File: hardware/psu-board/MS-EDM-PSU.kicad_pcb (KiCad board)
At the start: 4 copper layers, 150 x 95 mm, 42 parts, among them J1 HV_DC_IN__60-120V, J2 GAP_OUT__wire_work, J3 CAN, J4 LOGIC_5V_IN, J5 SWD, J6 NTC_TEMP, Q1 SiC_MOSFET, U1 STM32G474, U10 ISO_GATE_DRIVER, U11 ISO_CURRENT_AMP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

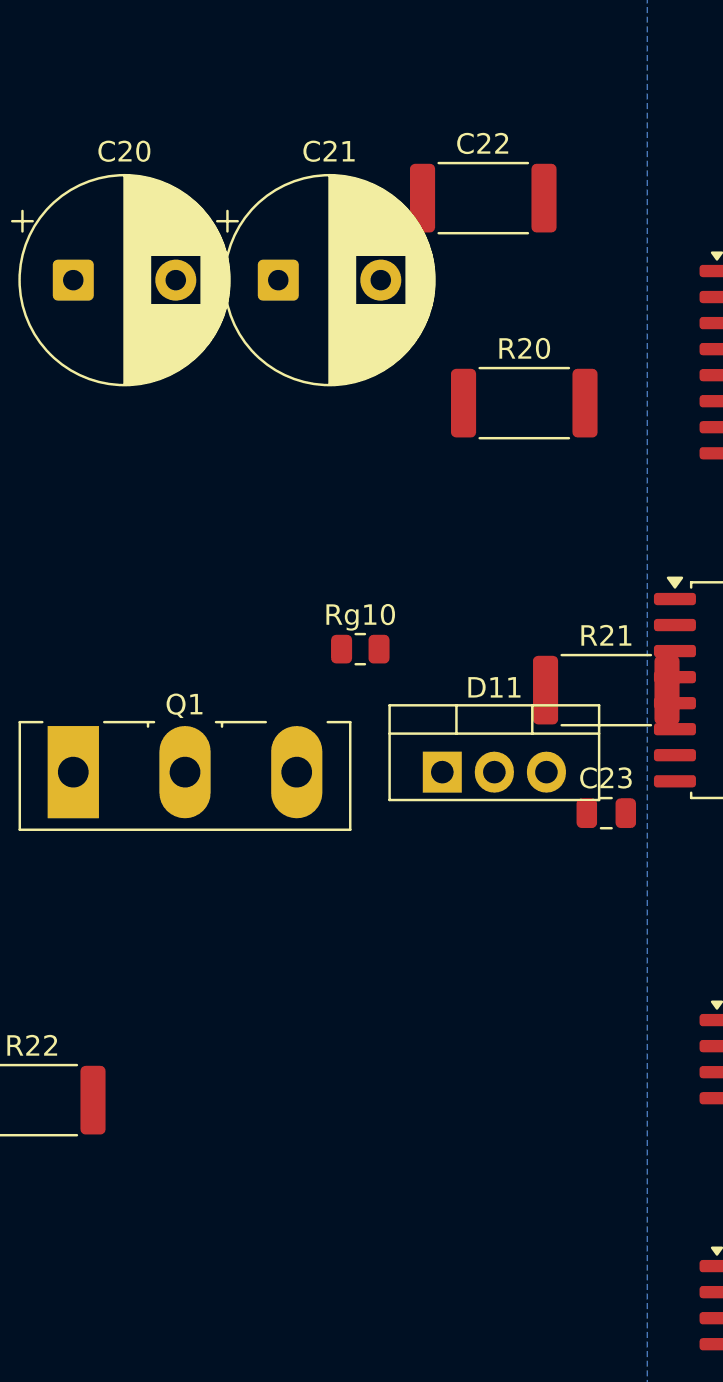
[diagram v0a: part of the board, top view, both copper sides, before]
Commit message: hw(psu): schematic-first PSU (real symbols, readable blocks, ERC 0 errors); retire PCB-only scaffold; keep HV review gate
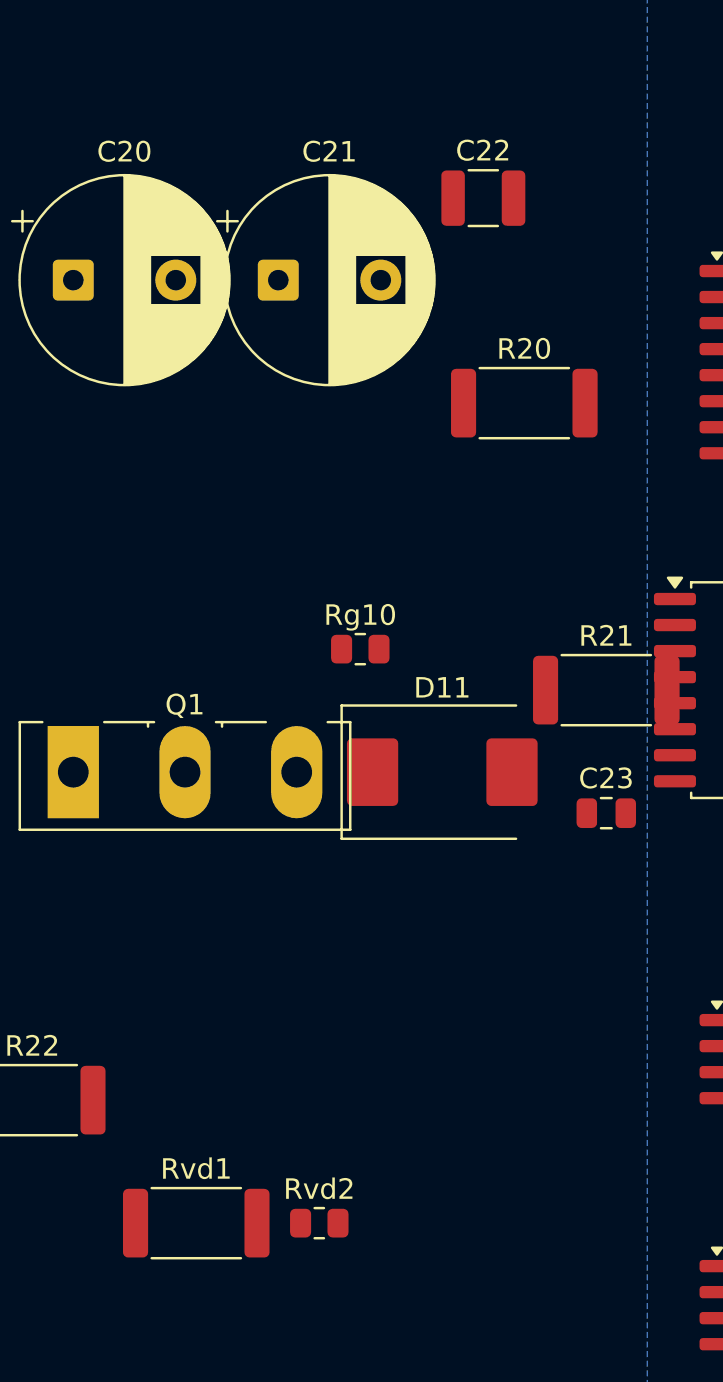
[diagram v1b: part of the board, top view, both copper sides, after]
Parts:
- added Rvd1: 1M_HVdiv, R_2512_6332Metric, F.Cu at (36.0, 66.0)
- added Rvd2: 3k9_HVdiv, R_0805_2012Metric, F.Cu at (42.0, 66.0)
- C20, C21: value bulk_220uF -> 220uF
- C22: value film_1uF -> 1uF_film; footprint R_2512_6332Metric -> C_1210_3225Metric
- D11: footprint TO-220-3_Vertical -> D_SMC
- F1: value FUSE_placeholder -> FUSE
- J1: value HV_DC_IN__60-120V -> HV_DC_IN_60-120V
- J2: value GAP_OUT__wire_work -> GAP_OUT_wire_work
- R20: value bleeder -> 100k_bleed
- R22: value shunt_R -> 5mR_shunt
- R3: value 120R_term -> 120R
- Rg10: value gate_R -> 10R_gate
- U1: value STM32G474 -> STM32G474CBTx
- U2: value TJA1051 -> TJA1051T-3
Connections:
- C1 pad 2: GNDL -> GND
- C2 pad 2: GNDL -> GND
- C23 pad 2: SNUB_G -> HV-
- C3 pad 2: GNDL -> GND
- C4 pad 2: GNDL -> GND
- C5 pad 2: GNDL -> GND
- C6 pad 2: GNDL -> GND
- C7 pad 2: GNDL -> GND
- D1 pad 1: RUN_R -> GND
- D1 pad 2: RUN -> RUN_LED
- D2 pad 1: FAULT_R -> GND
- D2 pad 2: FAULT -> FAULT_LED
- J3 pad 3: CAN_GND -> GND
- J4 pad 2: GNDL -> GND
- J5 pad 1: SWD_3V3 -> +3V3
- J5 pad 3: GNDL -> GND
- J6 pad 2: GNDL -> GND
- MH1 pad : GNDL -> GND
- MH2 pad : GNDL -> GND
- MH3 pad : GNDL -> GND
- MH4 pad : GNDL -> GND
- Q1 pad 1: SW_NODE -> GATE
- Q1 pad 2: HVF -> SW_NODE
- Q1 pad 3: (no net) -> HVF
- R22 pad 1: ISENSE_HV -> GAP_RTN
- R22 pad 2: ISENSE_HV_G -> HV-
- R4 pad 1: RUN_R -> RUN
- R4 pad 2: GNDL -> RUN_LED
- R5 pad 1: FAULT_R -> FAULT
- R5 pad 2: GNDL -> FAULT_LED
- Rg10 pad 2: SW_NODE -> GATE
- U1 pad 1: (no net) -> +3V3
- U1 pad 10: (no net) -> VSENSE_P
- U1 pad 11: ISENSE -> VSENSE_N
- U1 pad 12: VSENSE -> NTC_AIN
- U1 pad 14: NTC_AIN -> (no net)
- U1 pad 16: (no net) -> RUN
- U1 pad 17: (no net) -> FAULT
- U1 pad 19: (no net) -> GND
- U1 pad 20: (no net) -> +3V3
- U1 pad 21: (no net) -> +3V3
- U1 pad 23: GNDL -> GND
- U1 pad 26: GATE_PWM -> DIO_TX
- U1 pad 27: DIO_A -> DIO_RX
- U1 pad 28: DIO_B -> (no net)
- U1 pad 29: RUN -> (no net)
- U1 pad 30: FAULT -> GATE_PWM
- U1 pad 34: SWDIO -> (no net)
- U1 pad 35: GNDL -> GND
- U1 pad 37: SWCLK -> SWDIO
- U1 pad 38: (no net) -> SWCLK
- U1 pad 47: GNDL -> GND
- U1 pad 8: GNDL -> ISENSE_P
- U1 pad 9: +3V3 -> ISENSE_N
- U10 pad 1: (no net) -> GATE_PWM
- U10 pad 14: (no net) -> HV-
- U10 pad 15: (no net) -> GATE_DRV
- U10 pad 16: (no net) -> GDRV_VDD
- U10 pad 2: GATE_PWM -> (no net)
- U10 pad 3: (no net) -> +3V3
- U10 pad 4: (no net) -> GND
- U10 pad 5: (no net) -> GND
- U10 pad 6: (no net) -> +3V3
- U10 pad 8: (no net) -> +3V3
- U10 pad 9: GATE_DRV -> (no net)
- U11 pad 1: (no net) -> ISO_HV_VDD
- U11 pad 2: ISENSE_HV -> GAP_RTN
- U11 pad 3: ISENSE_HV_G -> HV-
- U11 pad 4: (no net) -> HV-
- U11 pad 5: (no net) -> GND
- U11 pad 6: ISENSE -> ISENSE_N
- U11 pad 7: (no net) -> ISENSE_P
- U11 pad 8: (no net) -> +3V3
- U12 pad 1: (no net) -> ISO_HV_VDD
- U12 pad 3: VSENSE_HV_G -> HV-
- U12 pad 4: (no net) -> HV-
- U12 pad 5: (no net) -> GND
- U12 pad 6: VSENSE -> VSENSE_N
- U12 pad 7: (no net) -> VSENSE_P
- U12 pad 8: (no net) -> +3V3
- U13 pad 1: (no net) -> +3V3
- U13 pad 14: (no net) -> DIO_RX
- U13 pad 15: DIO_B -> HV-
- U13 pad 16: (no net) -> ISO_HV_VDD
- U13 pad 2: DIO_A -> GND
- U13 pad 3: (no net) -> DIO_TX
- U13 pad 8: (no net) -> GND
- U13 pad 9: (no net) -> HV-
- U2 pad 2: GNDL -> GND
- U2 pad 8: GNDL -> GND
- U3 pad 1: GNDL -> GND
- Y1 pad 2: Y1_G -> GND
- Y1 pad 4: Y1_G -> GND
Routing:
- added copper zone on B.Cu, net GND
- added copper zone on In2.Cu, net GND
- removed copper zone on B.Cu, net GNDL
- removed copper zone on In2.Cu, net GNDL
